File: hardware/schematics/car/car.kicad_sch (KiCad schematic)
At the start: 22 parts, among them M1 Motor_Servo, Q1 PMOS, SW1 SW_SPST, SW2 SW_Push, SW3 SW_Push, U1 VL53L0CXV0DH1, U10 Mini-560, U11 JGA25-37x, U2 VL53L0CXV0DH1, U3 VL53L0CXV0DH1, U4 Pixy2, U6 TB6612FNG, U7 SparkFun OTOS, U8 SWD debug probe, U9 Mini-360

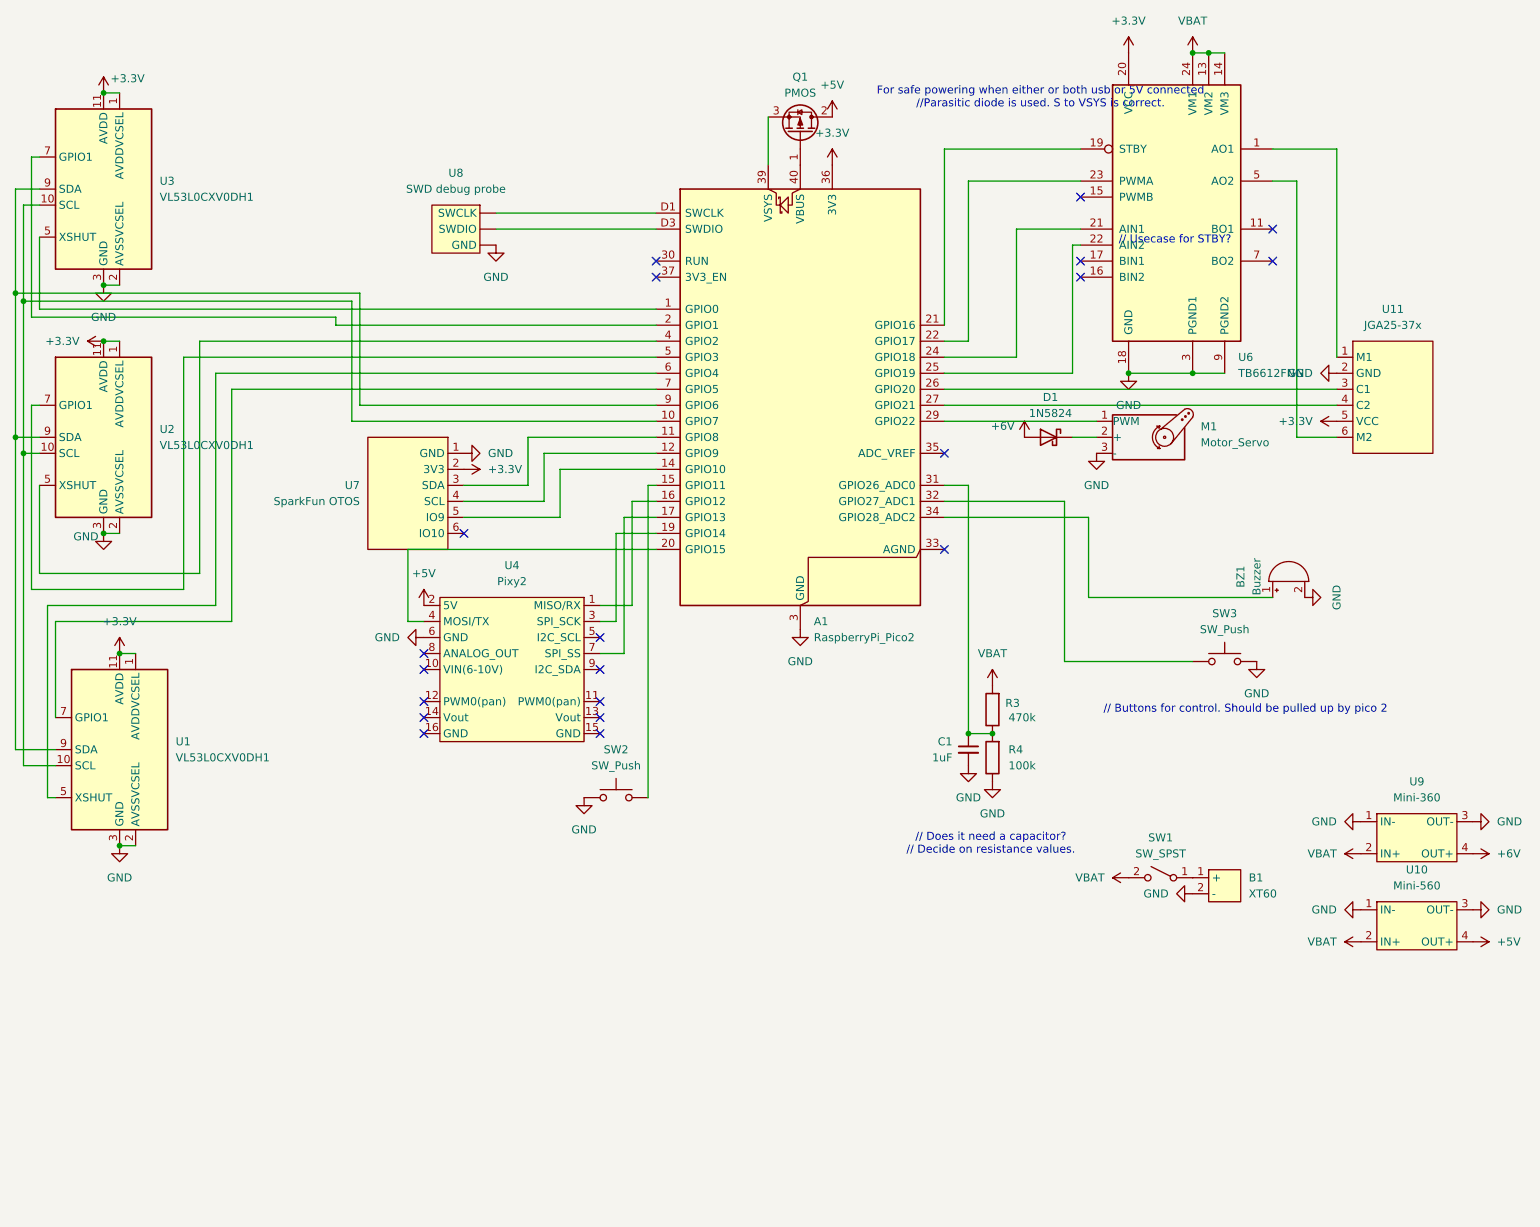
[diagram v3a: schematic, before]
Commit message: [Schematic] Move a lot, fix mini560 footprint wrong size.
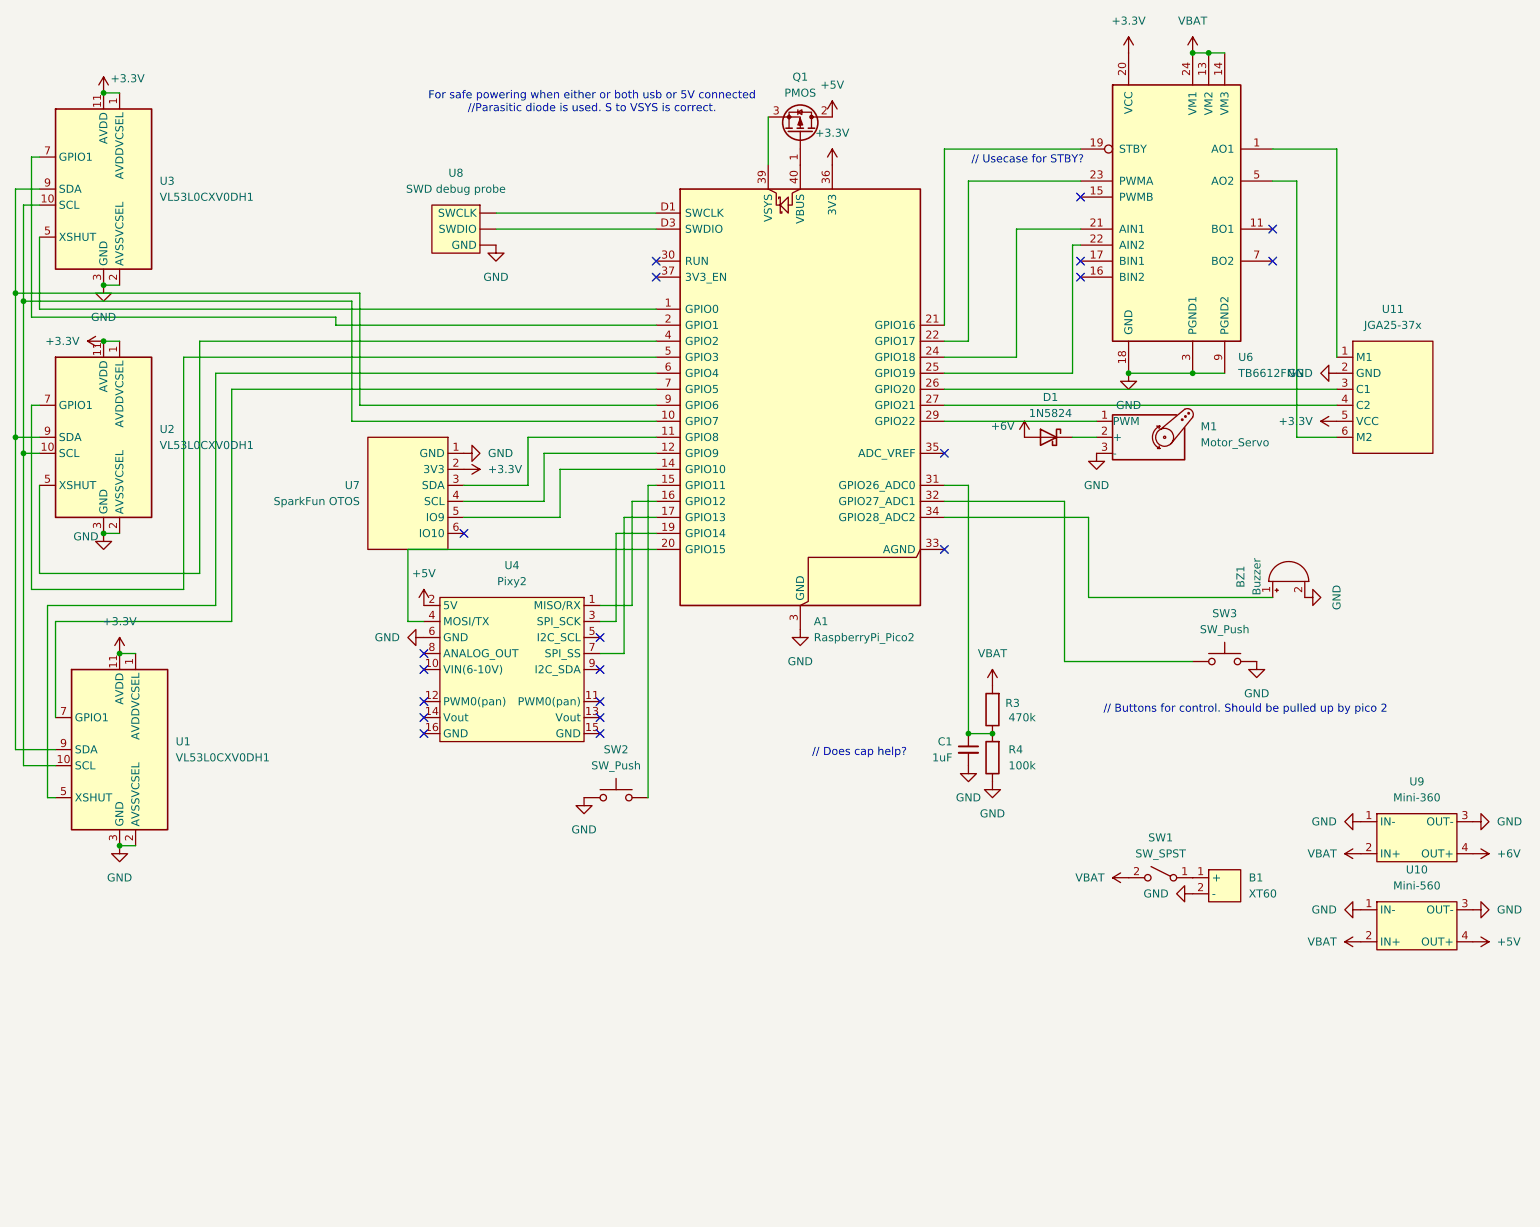
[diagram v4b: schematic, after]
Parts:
- U11: footprint Connector_PinHeader_2.54mm:PinHeader_1x06_P2.54mm_Vertical -> xlnc-foot:JGA25-37x_PinHeader_1x06_P2.54mm_Vertical
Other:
- note added: "// Does cap help?"
- note removed: "// Does it need a capacitor? // Decide on resistance values."
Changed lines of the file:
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@@
 	(text "For safe powering when either or both usb or 5V connected\n//Parasitic diode is used. S to VSYS is correct."
 		(exclude_from_sim yes)
-		(at 179.07 18.542 0)
+		(at 107.95 19.304 0)
 		(effects
 			(font
@@
 	(text "// Usecase for STBY?"
 		(exclude_from_sim no)
-		(at 200.406 41.148 0)
+		(at 177.038 28.448 0)
 		(effects
 			(font
@@
 		)
 	)
-	(text "// Does it need a capacitor?\n// Decide on resistance values."
+	(text "// Does cap help?"
 		(exclude_from_sim no)
-		(at 171.196 136.906 0)
+		(at 150.368 122.428 0)
 		(effects
 			(font
@@
 			)
 		)
-		(property "Datasheet" "https://toshiba.semicon-storage.com/info/TB6612FNG_datasheet_en_20141001.pdf?did=10660&prodName=TB6612FNG"
+		(property "Datasheet" "https://toshiba.semicon-storage.com/us/product/linear/motordriver/detail.TB6612FNG.html"
 			(at 212.09 21.59 0)
 			(hide yes)
@@
 			)
 		)
-		(property "Footprint" "Connector_PinHeader_2.54mm:PinHeader_1x06_P2.54mm_Vertical"
+		(property "Footprint" "xlnc-foot:JGA25-37x_PinHeader_1x06_P2.54mm_Vertical"
 			(at 228.6 66.04 0)
 			(hide yes)

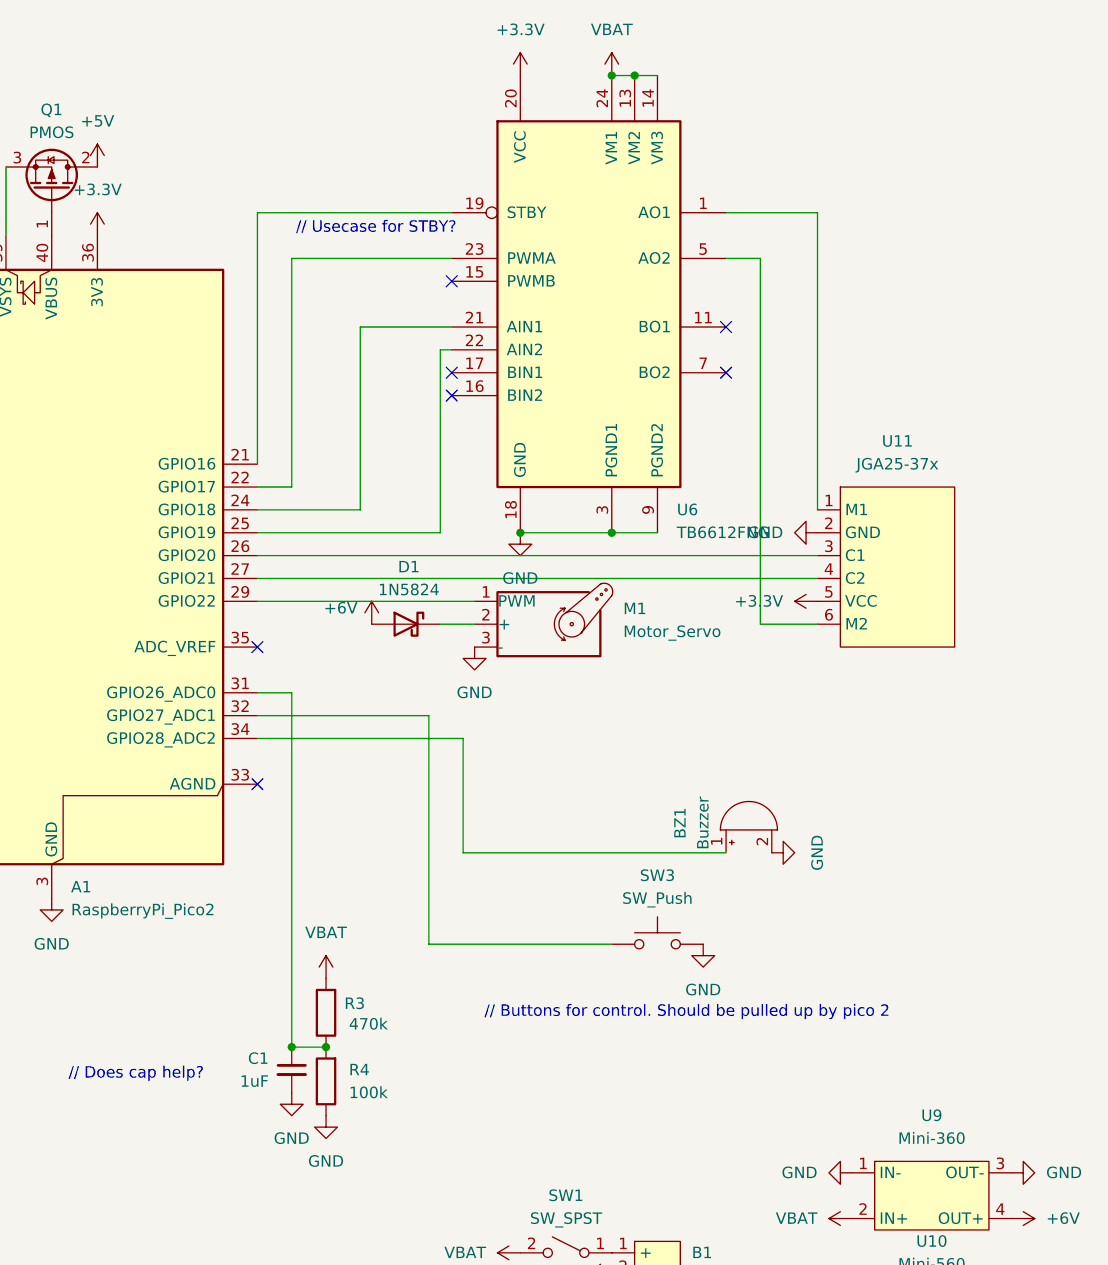
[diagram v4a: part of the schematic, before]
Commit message: [Schematic] Routed all.
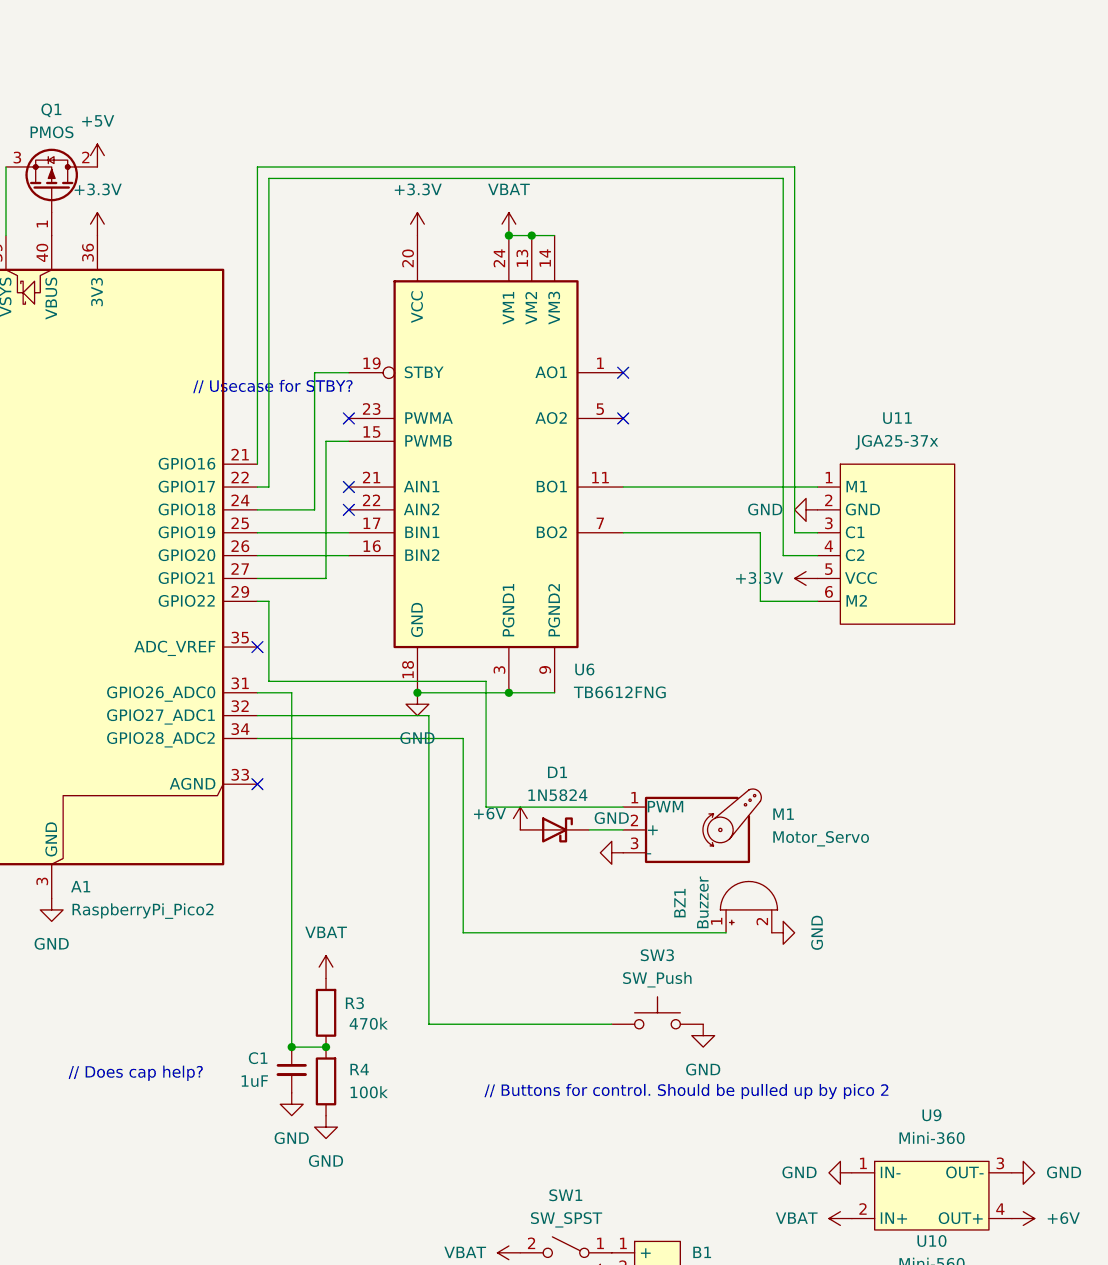
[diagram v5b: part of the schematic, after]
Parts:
- U9: footprint xlnc-foot:Buck_Mini-360 -> xlnc-foot:Buck_Mini-360_2.54mm
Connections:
- net at U6.1 (AO1), U6.2 (AO1): no longer U11.1 (M1)
- net at U6.11 (BO1), U6.12 (BO1): now also U11.1 (M1)
- net at U6.15 (PWMB): now also A1.27 (GPIO21)
- net at U6.16 (BIN2): now also A1.26 (GPIO20)
- net at U6.17 (BIN1): now also A1.25 (GPIO19)
- net at U6.19 (STBY): now also A1.24 (GPIO18); no longer A1.21 (GPIO16)
- net at U6.21 (AIN1): no longer A1.24 (GPIO18)
- net at U6.22 (AIN2): no longer A1.25 (GPIO19)
- net at U6.23 (PWMA): no longer A1.22 (GPIO17)
- net at U6.5 (AO2), U6.6 (AO2): no longer U11.6 (M2)
- net at U6.7 (BO2), U6.8 (BO2): now also U11.6 (M2)
- net at U11.3 (C1): now also A1.21 (GPIO16); no longer A1.26 (GPIO20)
- net at U11.4 (C2): now also A1.22 (GPIO17); no longer A1.27 (GPIO21)
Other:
- moved on the sheet: BZ1, D1, M1, SW3, U11, U6

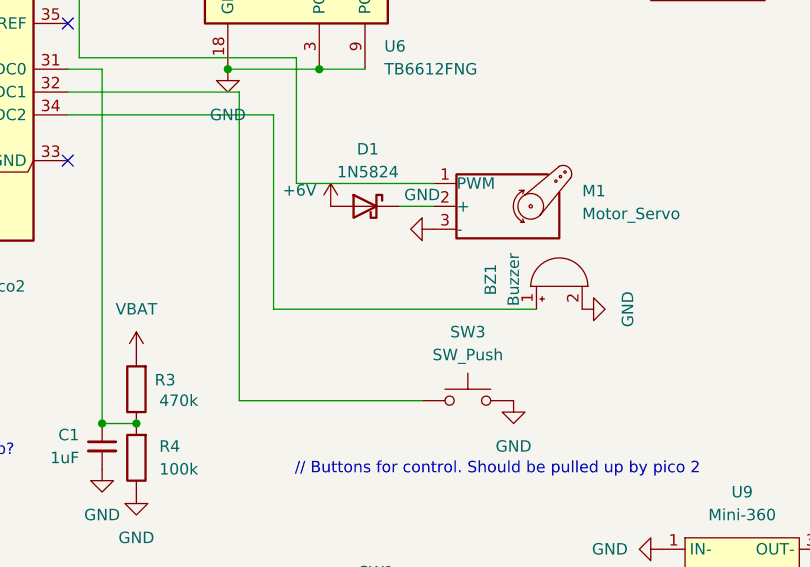
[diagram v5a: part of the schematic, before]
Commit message: [Schematic] Add 200ohm R in series with buzzer to limit current.
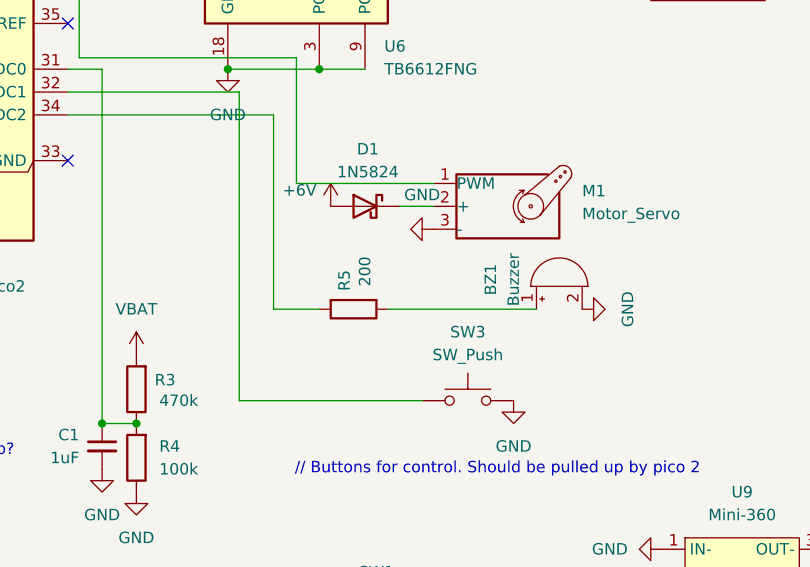
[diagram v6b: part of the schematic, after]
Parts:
- added R5: 200, Resistor_THT:R_Axial_DIN0204_L3.6mm_D1.6mm_P2.54mm_Vertical, symbol Device:R
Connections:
- net at BZ1.1 (+): now also R5.1; no longer A1.34 (GPIO28_ADC2)
- new net: A1.34 (GPIO28_ADC2), R5.2
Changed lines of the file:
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@@
 	(wire
 		(pts
-			(xy 186.69 106.68) (xy 215.9 106.68)
+			(xy 186.69 106.68) (xy 191.77 106.68)
 		)
 		(stroke
@@
 	(wire
 		(pts
+			(xy 199.39 106.68) (xy 215.9 106.68)
+		)
+		(stroke
+			(width 0)
+			(type default)
+		)
+	)
+	(wire
+		(pts
 			(xy 186.69 106.68) (xy 186.69 85.09)
 		)
@@
 					(unit 1)
 				)
+			)
+		)
+	)
+	(symbol
+		(lib_id "Device:R")
+		(at 195.58 106.68 270)
+		(unit 1)
+		(body_style 1)
+		(exclude_from_sim no)
+		(in_bom yes)
+		(on_board yes)
+		(in_pos_files yes)
+		(dnp no)
+		(property "Reference" "R5"
+			(at 194.564 104.648 0)
+			(show_name no)
+			(do_not_autoplace no)
+			(effects
+				(font
+					(size 1.27 1.27)
+				)
+				(justify right)
+			)
+		)
+		(property "Value" "200"
+			(at 196.8499 104.14 0)
+			(show_name no)
+			(do_not_autoplace no)
+			(effects
+				(font
+					(size 1.27 1.27)
+				)
+				(justify right)
+			)
+		)
+		(property "Footprint" "Resistor_THT:R_Axial_DIN0204_L3.6mm_D1.6mm_P2.54mm_Vertical"
+			(at 195.58 104.902 90)
+			(hide yes)
+			(show_name no)
+			(do_not_autoplace no)
+			(effects
+				(font
+					(size 1.27 1.27)
+				)
+			)
+		)
+		(property "Datasheet" ""
+			(at 195.58 106.68 0)
+			(hide yes)
+			(show_name no)
+			(do_not_autoplace no)
+			(effects
+				(font
+					(size 1.27 1.27)
+				)
+			)
+		)
+		(property "Description" "Resistor"
+			(at 195.58 106.68 0)
+			(hide yes)
+			(show_name no)
+			(do_not_autoplace no)
+			(effects
+				(font
+					(size 1.27 1.27)
+				)
+			)
+		)
+		(pin "2"
+		)
+		(pin "1"
+		)
+		(instances
+			(project "car"
+				(path "/5e1ba60a-5dff-4ce7-a8b0-cf19f27fe16e"
+					(reference "R5")
+					(unit 1)
+				)
